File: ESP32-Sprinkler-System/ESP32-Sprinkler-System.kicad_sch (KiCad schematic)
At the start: 13 parts, among them J104 DHT

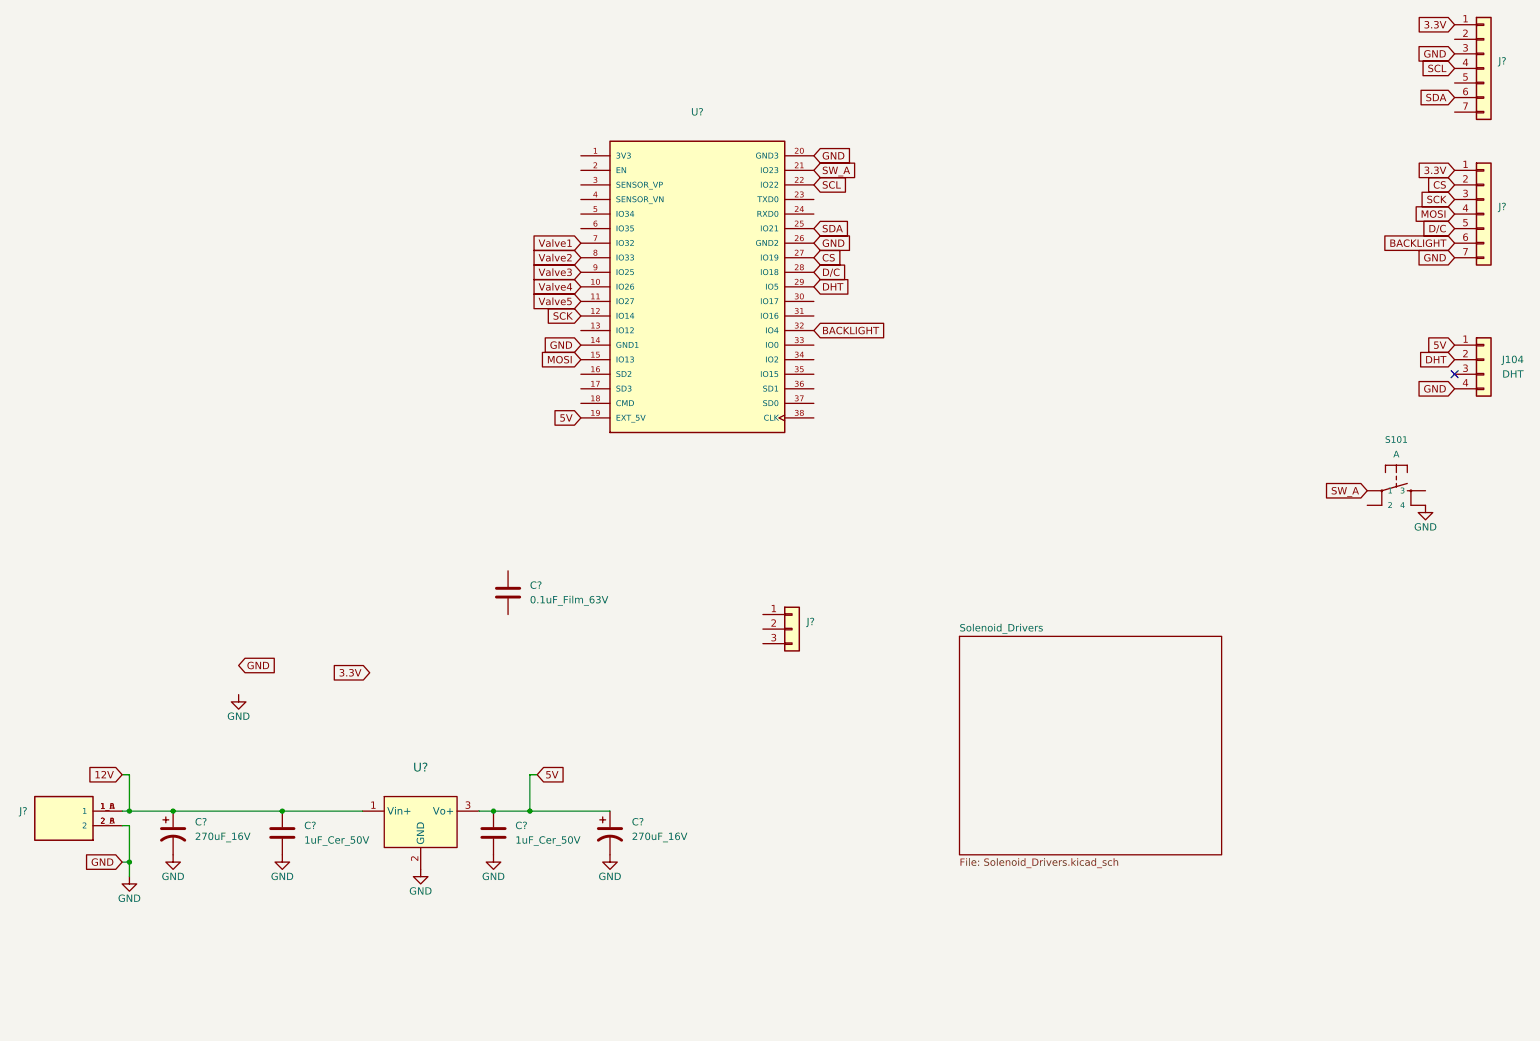
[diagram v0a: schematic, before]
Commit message: Schematic done, footprints assigned, terminal block requires footprint clarity, some 3D models missing.
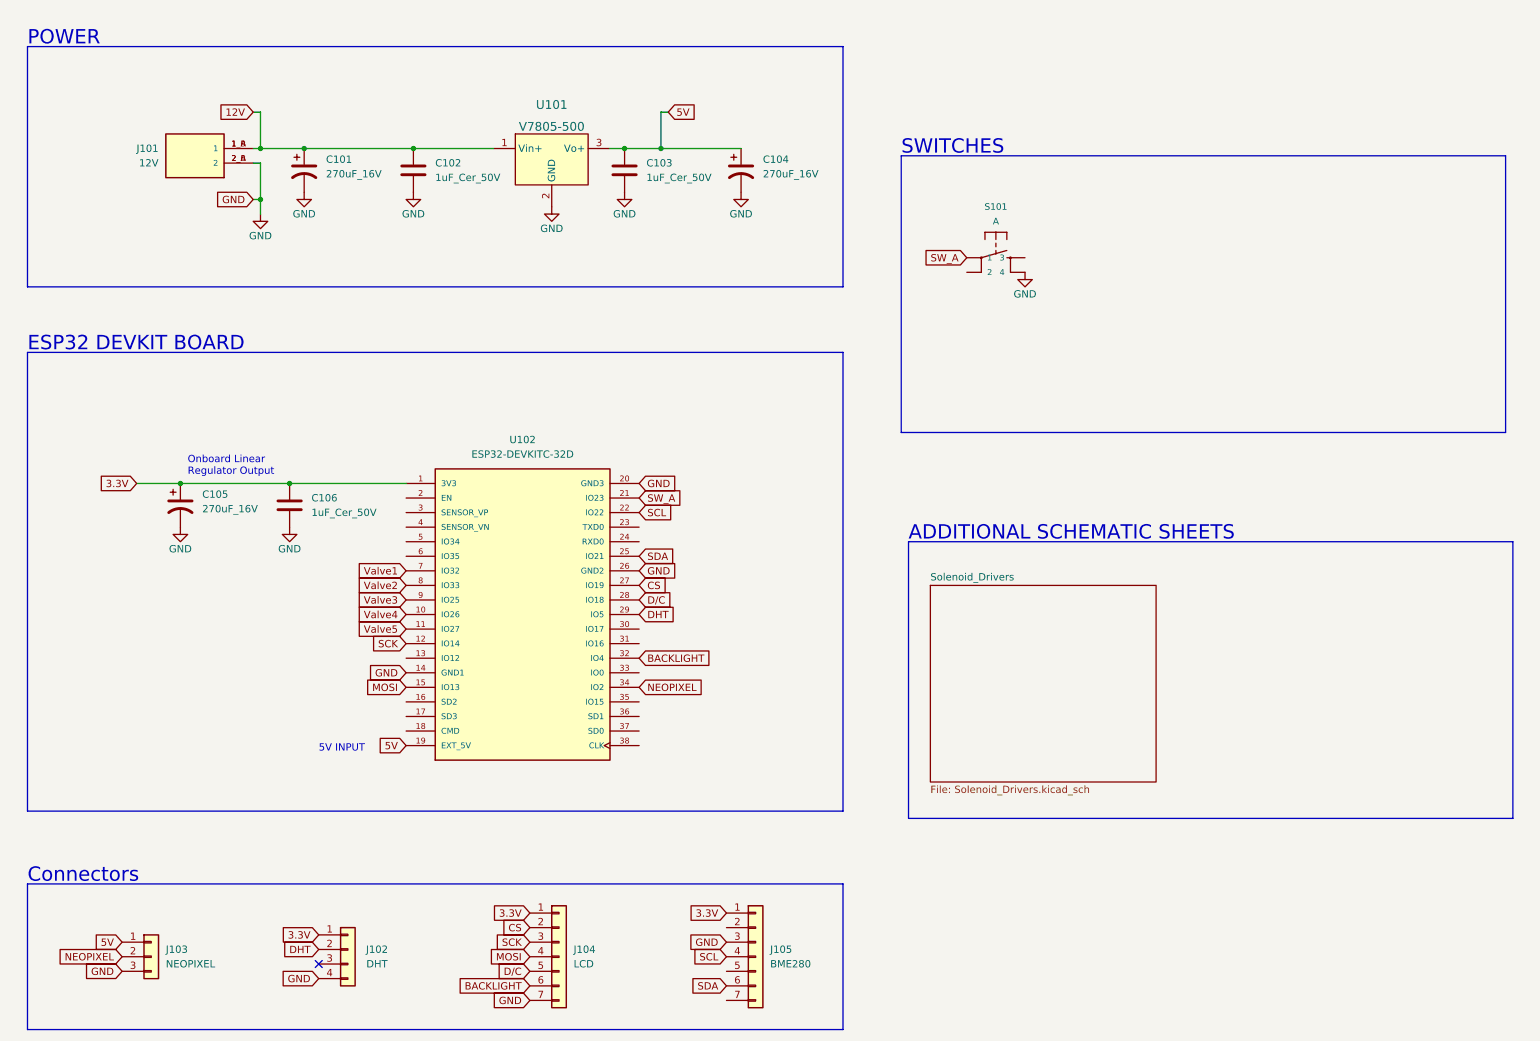
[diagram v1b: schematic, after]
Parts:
- removed C?: 0.1uF_Film_63V, Capacitor_THT:C_Rect_L7.0mm_W2.5mm_P5.00mm, symbol Device:C
- added C105: 270uF_16V, Capacitor_THT:CP_Radial_D6.3mm_P2.50mm, symbol Device:C_Polarized_US
- added C106: 1uF_Cer_50V, Capacitor_THT:C_Disc_D7.5mm_W4.4mm_P5.00mm, symbol Device:C
- J101: renamed from J?; value (none) -> 12V
- J103: renamed from J?; value (none) -> NEOPIXEL
- J104: renamed from J?; value (none) -> LCD
- J105: renamed from J?; value (none) -> BME280
- U101: renamed from U?; value (none) -> V7805-500; footprint (none) -> digikey-footprints:3-SIP_Module_V7805-500
- U102: renamed from U?; value (none) -> ESP32-DEVKITC-32D
- gave numbers to parts that had none: 4
- renumbered J104 to J102
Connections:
- net 3.3V: now also J102.1 (Pin_1), U102.1 (3V3), C105.1, C106.1
- net 5V: now also J103.1 (Pin_1); no longer J102.1 (Pin_1)
- net GND: now also J103.3 (Pin_3), C105.2, C106.2
- net NEOPIXEL: now reaches U102.34 (IO2)
- net NEOPIXEL: now also J103.2 (Pin_2)
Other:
- note added: "5V INPUT"
- note added: "ADDITIONAL SCHEMATIC SHEETS"
- note added: "Connectors"
- note added: "ESP32 DEVKIT BOARD"
- note added: "Onboard Linear Regulator Output"
- note added: "POWER"
- note added: "SWITCHES"
- moved on the sheet: C101, C102, C103, C104, J101, J102, J103, J104, J105, S101, U101, U102

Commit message: Objs sorted like the schematic
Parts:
- J102: footprint (none) -> Connector_PinSocket_2.54mm:PinSocket_1x04_P2.54mm_Vertical
- J103: footprint (none) -> Connector_PinSocket_2.54mm:PinSocket_1x03_P2.54mm_Vertical
- J104, J105: footprint (none) -> Connector_PinSocket_2.54mm:PinSocket_1x07_P2.54mm_Vertical
- U102: footprint (none) -> ESP32-DEVKITC-32D:MODULE_ESP32-DEVKITC-32D
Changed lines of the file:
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@@
     (property "Reference" "U102" (id 0) (at 105.41 87.63 0))
     (property "Value" "ESP32-DEVKITC-32D" (id 1) (at 105.41 90.17 0))
-    (property "Footprint" "" (id 2) (at 105.41 118.11 0)
+    (property "Footprint" "ESP32-DEVKITC-32D:MODULE_ESP32-DEVKITC-32D" (id 2) (at 105.41 118.11 0)
       (effects (font (size 1.27 1.27)) (justify left bottom) hide)
     )
@@
       (effects (font (size 1.27 1.27)) (justify left))
     )
-    (property "Footprint" "" (id 2) (at 146.05 177.8 0)
+    (property "Footprint" "Connector_PinSocket_2.54mm:PinSocket_1x07_P2.54mm_Vertical" (id 2) (at 146.05 177.8 0)
       (effects (font (size 1.27 1.27)) hide)
     )
@@
     (property "Reference" "J102" (id 0) (at 80.01 176.53 0))
     (property "Value" "DHT" (id 1) (at 80.01 179.07 0))
-    (property "Footprint" "" (id 2) (at 74.93 176.53 0)
+    (property "Footprint" "Connector_PinSocket_2.54mm:PinSocket_1x04_P2.54mm_Vertical" (id 2) (at 74.93 176.53 0)
       (effects (font (size 1.27 1.27)) hide)
     )
@@
       (effects (font (size 1.27 1.27)) (justify left))
     )
-    (property "Footprint" "" (id 2) (at 40.64 177.8 0)
+    (property "Footprint" "Connector_PinSocket_2.54mm:PinSocket_1x03_P2.54mm_Vertical" (id 2) (at 40.64 177.8 0)
       (effects (font (size 1.27 1.27)) hide)
     )
@@
       (effects (font (size 1.27 1.27)) (justify left))
     )
-    (property "Footprint" "" (id 2) (at 111.76 177.8 0)
-      (effects (font (size 1.27 1.27)) hide)
-    )
+    (property "Footprint" "Connector_PinSocket_2.54mm:PinSocket_1x07_P2.54mm_Vertical" (id 2) (at 111.76 177.8 0)
+      (effects (font (size 1.27 1.27)) hide)
+    )

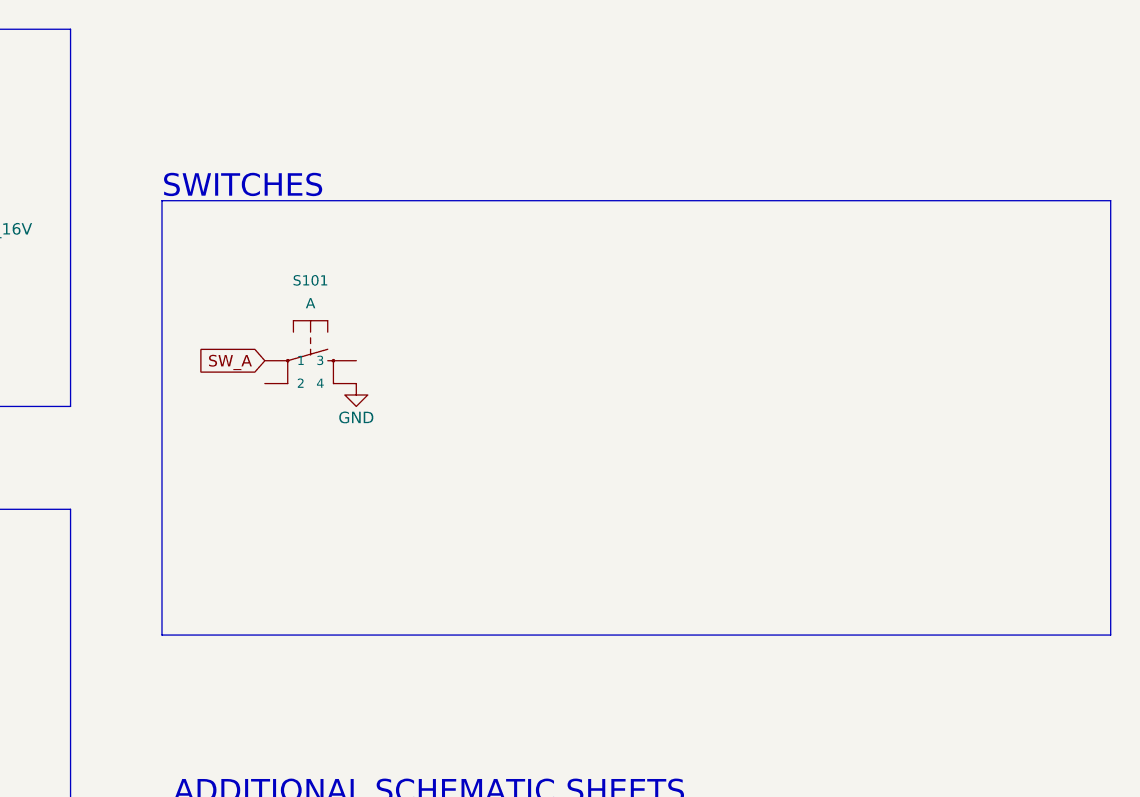
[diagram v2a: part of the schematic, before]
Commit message: Added M3 Mounting Holes
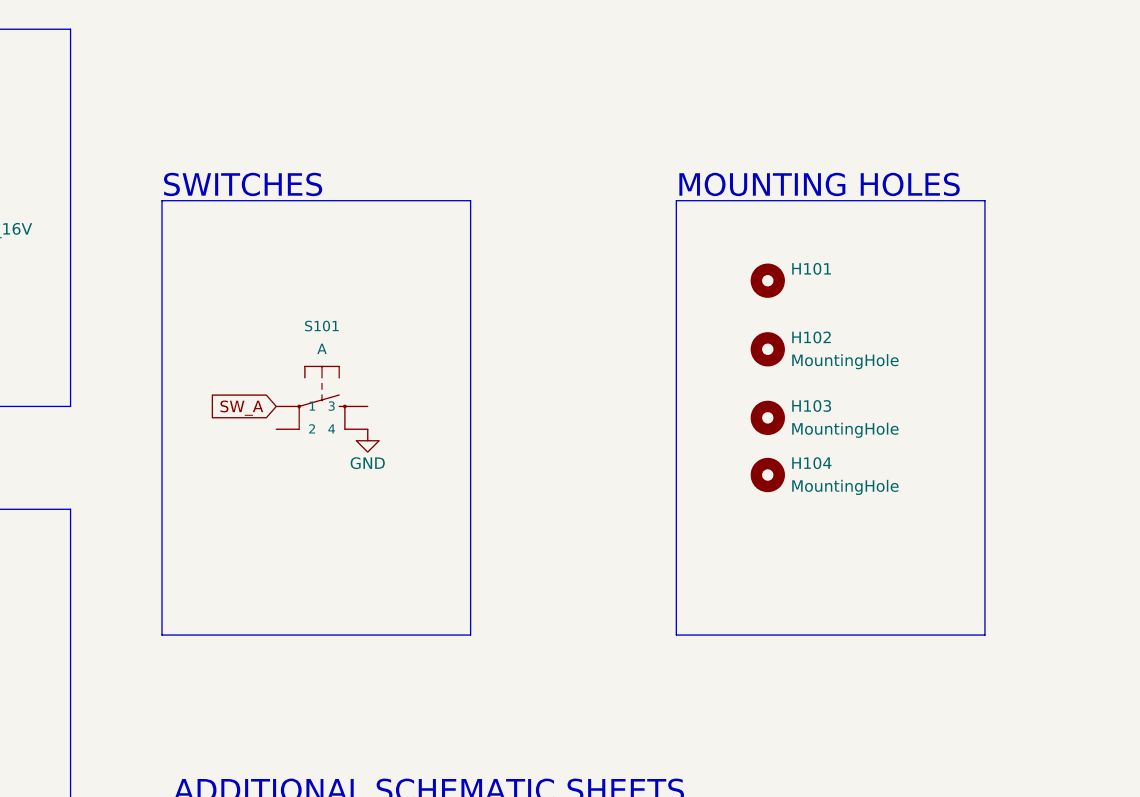
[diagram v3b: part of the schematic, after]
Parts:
- added H101: (no value), symbol Mechanical:MountingHole
- added H102, H103, H104: MountingHole, MountingHole:MountingHole_3.2mm_M3, symbol Mechanical:MountingHole
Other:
- note added: "MOUNTING HOLES"
- moved on the sheet: S101
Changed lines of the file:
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@@
     (stroke (width 0) (type default) (color 0 0 0 0))
   )
-  (polyline (pts (xy 276.86 86.36) (xy 276.86 38.1))
+  (polyline (pts (xy 205.74 86.36) (xy 205.74 38.1))
     (stroke (width 0) (type default) (color 0 0 0 0))
   )
@@
     (stroke (width 0) (type default) (color 0 0 0 0))
   )
-  (polyline (pts (xy 276.86 38.1) (xy 171.45 38.1))
+  (polyline (pts (xy 205.74 38.1) (xy 171.45 38.1))
     (stroke (width 0) (type default) (color 0 0 0 0))
   )
@@
     (stroke (width 0) (type default) (color 0 0 0 0))
   )
+  (polyline (pts (xy 262.89 38.1) (xy 228.6 38.1))
+    (stroke (width 0) (type default) (color 0 0 0 0))
+  )
   (wire (pts (xy 58.42 36.83) (xy 59.69 36.83))
     (stroke (width 0) (type default) (color 0 0 0 0))
@@
     (stroke (width 0) (type default) (color 0 0 0 0))
   )
+  (polyline (pts (xy 228.6 38.1) (xy 228.6 86.36))
+    (stroke (width 0) (type default) (color 0 0 0 0))
+  )
   (wire (pts (xy 58.42 39.37) (xy 59.69 39.37))
     (stroke (width 0) (type default) (color 0 0 0 0))
   )
-  (polyline (pts (xy 171.45 86.36) (xy 276.86 86.36))
+  (polyline (pts (xy 262.89 86.36) (xy 262.89 38.1))
+    (stroke (width 0) (type default) (color 0 0 0 0))
+  )
+  (polyline (pts (xy 171.45 86.36) (xy 205.74 86.36))
     (stroke (width 0) (type default) (color 0 0 0 0))
   )
@@
     (stroke (width 0) (type default) (color 0 0 0 0))
   )
+  (polyline (pts (xy 228.6 86.36) (xy 262.89 86.36))
+    (stroke (width 0) (type default) (color 0 0 0 0))
+  )
   (wire (pts (xy 130.81 30.48) (xy 129.54 30.48))
     (stroke (width 0) (type default) (color 0 0 0 0))
@@
   )
   (text "SWITCHES" (at 171.45 38.1 0)
+    (effects (font (size 2.5 2.5)) (justify left bottom))
+  )
+  (text "MOUNTING HOLES" (at 228.6 38.1 0)
     (effects (font (size 2.5 2.5)) (justify left bottom))
   )
@@
     )
   )
-  (global_label "SW_A" (shape input) (at 182.88 55.88 180) (fields_autoplaced)
-    (effects (font (size 1.27 1.27)) (justify right))
-    (property "Intersheet References" "${INTERSHEET_REFS}" (id 0) (at 175.7498 55.9594 0)
+  (global_label "SW_A" (shape input) (at 184.15 60.96 180) (fields_autoplaced)
+    (effects (font (size 1.27 1.27)) (justify right))
+    (property "Intersheet References" "${INTERSHEET_REFS}" (id 0) (at 177.0198 61.0394 0)
       (effects (font (size 1.27 1.27)) (justify right) hide)
     )
@@
     (pin "1")
   )
-  (symbol (lib_id "power:GND") (at 193.04 58.42 0) (unit 1)
+  (symbol (lib_id "Mechanical:MountingHole") (at 238.76 46.99 0) (unit 1)
+    (in_bom yes) (on_board yes) (fields_autoplaced)
+    (property "Reference" "H101" (id 0) (at 241.3 45.7199 0)
+      (effects (font (size 1.27 1.27)) (justify left))
+    )
+    (property "Value" "" (id 1) (at 241.3 48.2599 0)
+      (effects (font (size 1.27 1.27)) (justify left))
+    )
+    (property "Footprint" "" (id 2) (at 238.76 46.99 0)
+      (effects (font (size 1.27 1.27)) hide)
+    )
+    (property "Datasheet" "~" (id 3) (at 238.76 46.99 0)
+      (effects (font (size 1.27 1.27)) hide)
+    )
+  )
+  (symbol (lib_id "power:GND") (at 194.31 63.5 0) (unit 1)
     (in_bom yes) (on_board yes)
-    (property "Reference" "#PWR0107" (id 0) (at 193.04 64.77 0)
-      (effects (font (size 1.27 1.27)) hide)
-    )
-    (property "Value" "GND" (id 1) (at 193.04 62.23 0))
-    (property "Footprint" "" (id 2) (at 193.04 58.42 0)
-      (effects (font (size 1.27 1.27)) hide)
-    )
-    (property "Datasheet" "" (id 3) (at 193.04 58.42 0)
-      (effects (font (size 1.27 1.27)) hide)
-    )
-    (pin "1")
+    (property "Reference" "#PWR0107" (id 0) (at 194.31 69.85 0)
+      (effects (font (size 1.27 1.27)) hide)
+    )
+    (property "Value" "GND" (id 1) (at 194.31 67.31 0))
+    (property "Footprint" "" (id 2) (at 194.31 63.5 0)
+      (effects (font (size 1.27 1.27)) hide)
+    )
+    (property "Datasheet" "" (id 3) (at 194.31 63.5 0)
+      (effects (font (size 1.27 1.27)) hide)
+    )
+    (pin "1")
+  )
+  (symbol (lib_id "Mechanical:MountingHole") (at 238.76 62.23 0) (unit 1)
+    (in_bom yes) (on_board yes) (fields_autoplaced)
+    (property "Reference" "H103" (id 0) (at 241.3 60.9599 0)
+      (effects (font (size 1.27 1.27)) (justify left))
+    )
+    (property "Value" "MountingHole" (id 1) (at 241.3 63.4999 0)
+      (effects (font (size 1.27 1.27)) (justify left))
+    )
+    (property "Footprint" "MountingHole:MountingHole_3.2mm_M3" (id 2) (at 238.76 62.23 0)
+      (effects (font (size 1.27 1.27)) hide)
+    )
+    (property "Datasheet" "~" (id 3) (at 238.76 62.23 0)
+      (effects (font (size 1.27 1.27)) hide)
+    )
   )
   (symbol (lib_id "Device:C_Polarized_US") (at 143.51 40.64 0) (unit 1)
@@
     (pin "1")
   )
+  (symbol (lib_id "Mechanical:MountingHole") (at 238.76 54.61 0) (unit 1)
+    (in_bom yes) (on_board yes) (fields_autoplaced)
+    (property "Reference" "H102" (id 0) (at 241.3 53.3399 0)
+      (effects (font (size 1.27 1.27)) (justify left))
+    )
+    (property "Value" "MountingHole" (id 1) (at 241.3 55.8799 0)
+      (effects (font (size 1.27 1.27)) (justify left))
+    )
+    (property "Footprint" "MountingHole:MountingHole_3.2mm_M3" (id 2) (at 238.76 54.61 0)
+      (effects (font (size 1.27 1.27)) hide)
+    )
+    (property "Datasheet" "~" (id 3) (at 238.76 54.61 0)
+      (effects (font (size 1.27 1.27)) hide)
+    )
+  )
   (symbol (lib_id "Connector_Generic:Conn_01x03") (at 40.64 177.8 0) (unit 1)
     (in_bom yes) (on_board yes) (fields_autoplaced)
@@
     (pin "3")
   )
-  (symbol (lib_id "SparkFun-Switches:MOMENTARY-SWITCH-SPST-2-SMD-4.6X2.8MM") (at 187.96 55.88 0) (unit 1)
-    (in_bom yes) (on_board yes) (fields_autoplaced)
-    (property "Reference" "S101" (id 0) (at 187.96 46.99 0)
+  (symbol (lib_id "SparkFun-Switches:MOMENTARY-SWITCH-SPST-2-SMD-4.6X2.8MM") (at 189.23 60.96 0) (unit 1)
+    (in_bom yes) (on_board yes) (fields_autoplaced)
+    (property "Reference" "S101" (id 0) (at 189.23 52.07 0)
       (effects (font (size 1.143 1.143)))
     )
-    (property "Value" "A" (id 1) (at 187.96 49.53 0)
+    (property "Value" "A" (id 1) (at 189.23 54.61 0)
       (effects (font (size 1.143 1.143)))
     )
-    (property "Footprint" "Switches:TACTILE_SWITCH_PTH_12MM" (id 2) (at 187.96 49.53 0)
+    (property "Footprint" "Switches:TACTILE_SWITCH_PTH_12MM" (id 2) (at 189.23 54.61 0)
       (effects (font (size 0.508 0.508)) hide)
     )
-    (property "Datasheet" "" (id 3) (at 187.96 55.88 0)
-      (effects (font (size 1.27 1.27)) hide)
-    )
-    (property "Field4" "SWCH-13065" (id 4) (at 187.96 49.53 0)
+    (property "Datasheet" "" (id 3) (at 189.23 60.96 0)
+      (effects (font (size 1.27 1.27)) hide)
+    )
+    (property "Field4" "SWCH-13065" (id 4) (at 189.23 54.61 0)
       (effects (font (size 1.524 1.524)) hide)
     )
@@
     )
     (pin "1")
+  )
+  (symbol (lib_id "Mechanical:MountingHole") (at 238.76 68.58 0) (unit 1)
+    (in_bom yes) (on_board yes) (fields_autoplaced)
+    (property "Reference" "H104" (id 0) (at 241.3 67.3099 0)
+      (effects (font (size 1.27 1.27)) (justify left))
+    )
+    (property "Value" "MountingHole" (id 1) (at 241.3 69.8499 0)
+      (effects (font (size 1.27 1.27)) (justify left))
+    )
+    (property "Footprint" "MountingHole:MountingHole_3.2mm_M3" (id 2) (at 238.76 68.58 0)
+      (effects (font (size 1.27 1.27)) hide)
+    )
+    (property "Datasheet" "~" (id 3) (at 238.76 68.58 0)
+      (effects (font (size 1.27 1.27)) hide)
+    )
   )
   (symbol (lib_id "Device:C") (at 86.36 40.64 0) (unit 1)
@@
       (reference "D208") (unit 1) (value "SB240E-G") (footprint "Diode_THT:D_DO-15_P12.70mm_Horizontal")
     )
+    (path "/50d5a33d-196c-4902-9dbb-6aa4f73f9342"
+      (reference "H101") (unit 1) (value "MountingHole") (footprint "MountingHole:MountingHole_3.2mm_M3")
+    )
+    (path "/8907a62d-dc81-4d27-9597-dfd784b549cc"
+      (reference "H102") (unit 1) (value "MountingHole") (footprint "MountingHole:MountingHole_3.2mm_M3")
+    )
+    (path "/5600d29b-f665-422d-932c-b1ddf423f179"
+      (reference "H103") (unit 1) (value "MountingHole") (footprint "MountingHole:MountingHole_3.2mm_M3")
+    )
+    (path "/c768fc9c-4693-4ce2-a125-721f959abbf0"
+      (reference "H104") (unit 1) (value "MountingHole") (footprint "MountingHole:MountingHole_3.2mm_M3")
+    )
     (path "/fc09712c-2602-4d70-b634-6e9c4340da2e"
